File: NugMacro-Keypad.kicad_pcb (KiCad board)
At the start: 2 copper layers, 76.2 x 97.2 mm, 52 parts, among them J1 AVR-ISP-6, J2 Conn_01x04, J3 Conn_01x04_Female_For_LCD, SW1 SW_Push, SW2 RotaryEncoder_Switch, U1 ATmega32U4-A, Y1 16MHz

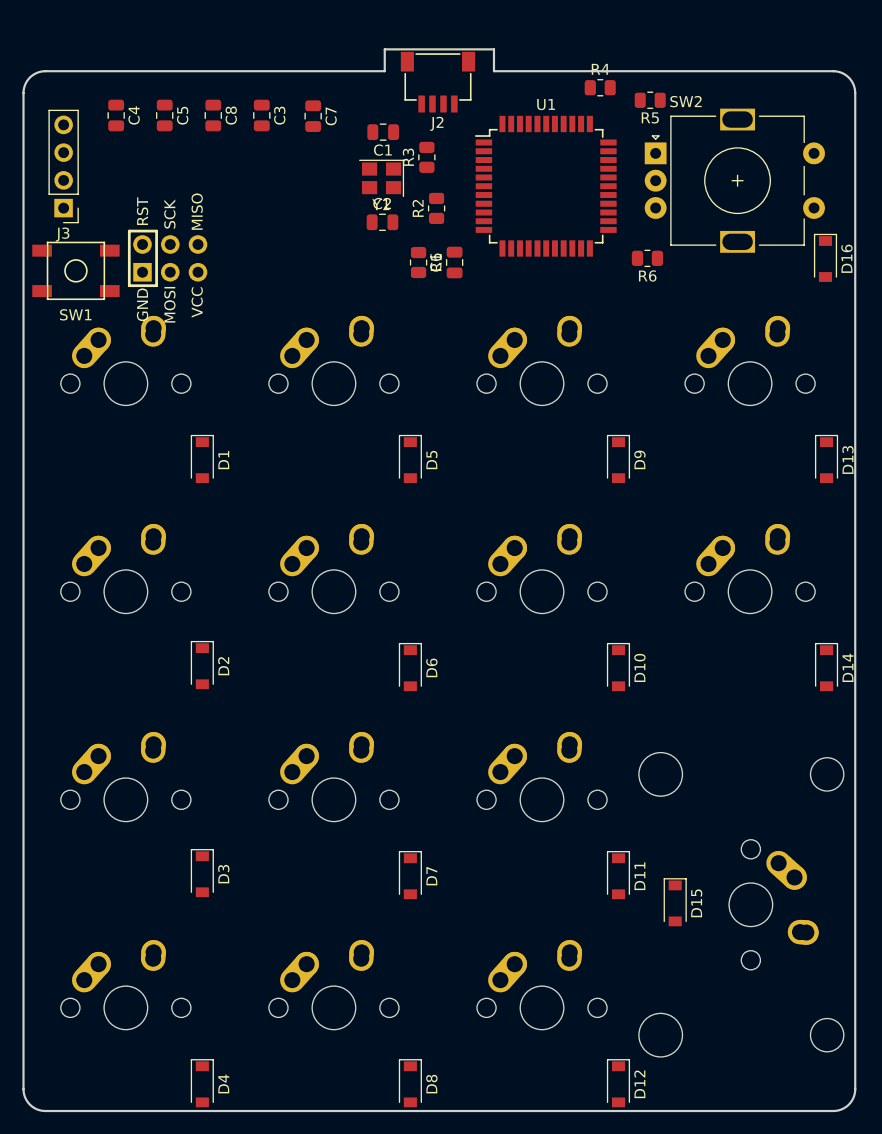
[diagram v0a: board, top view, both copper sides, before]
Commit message: lil schema and pcb changes
flipped/ changed around smd components so it may be easier to route, got rid of reset pins for simplicity sake with small board
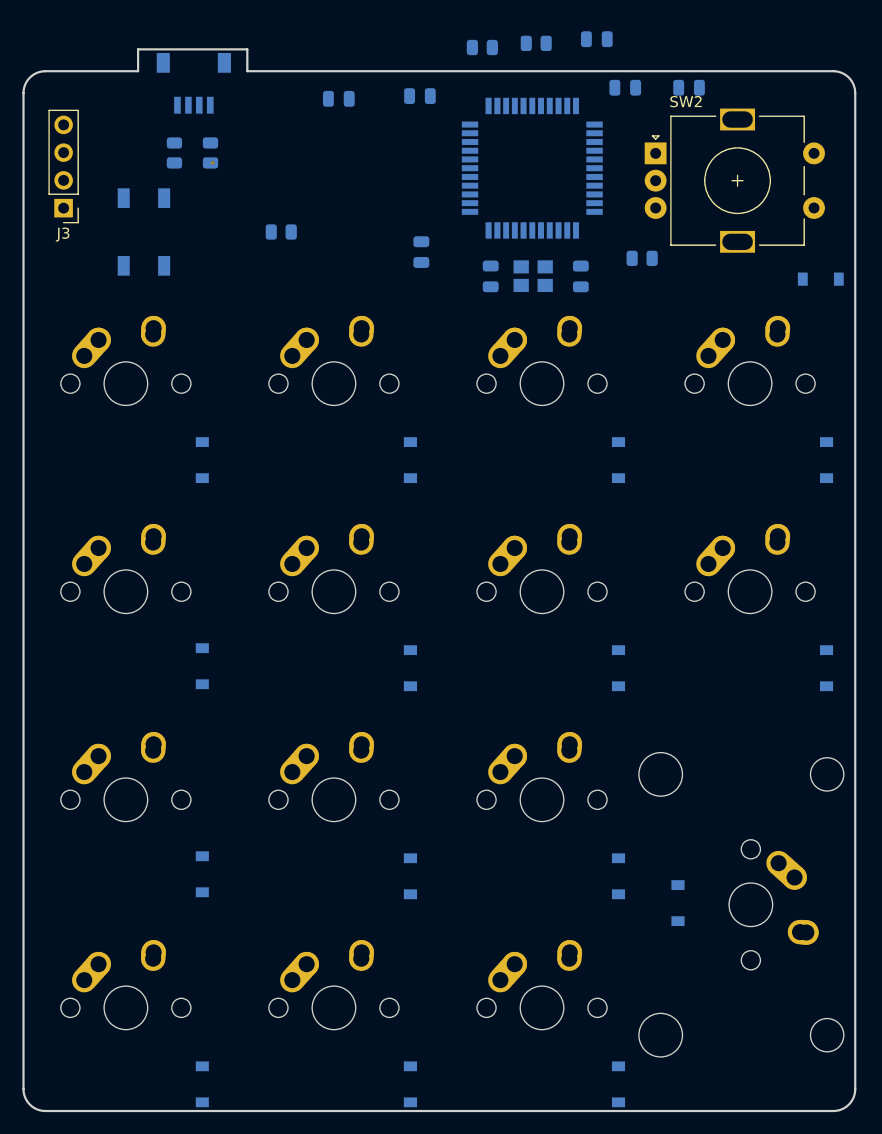
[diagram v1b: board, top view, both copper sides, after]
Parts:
- removed J1: AVR-ISP-6, random-keyboard-parts:Reset_Pretty-Mask
- C1, C2, C3, C4, C5, C6, C7, C8, D1, D10, D11, D12, D13, D14, D15, D16, D2, D3, D4, D5, D6, D7, D8, D9, J2, R1, R2, R3, R4, R5, R6, SW1, U1, Y1: moved to B.Cu
- moved C5 48.1 mm to (79.4, 57.3), turned to 180 degrees
- moved C3 31.5 mm to (70.9, 52.8), turned to 180 degrees
- moved C4 30.6 mm to (54.9, 72.3), turned to 90 degrees
- moved C7 28.7 mm to (73.5, 57.3), turned to 0 degrees
- moved R2 24.5 mm to (32.3, 63.2)
- moved J2 22.4 mm to (34.0, 54.1), turned to 0 degrees
- moved R3 19.8 mm to (35.6, 63.2)
- moved C2 18.8 mm to (69.5, 74.6), turned to 90 degrees
- moved Y1 16.5 mm to (65.1, 74.5)
- moved C1 16.5 mm to (61.2, 74.5), turned to -90 degrees
- moved R5 16.1 mm to (60.5, 53.6), turned to 0 degrees
- moved C6 15.6 mm to (54.7, 58.0), turned to 180 degrees
- moved R1 12.9 mm to (42.0, 70.5), turned to 180 degrees
- moved C8 11.6 mm to (47.3, 58.3), turned to 180 degrees
- moved SW1 7.17 mm to (29.5, 70.5), turned to 90 degrees
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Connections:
- net +5V renamed VCC
- U1 pad 10: MOSI -> unconnected-(U1-Pad10)
- U1 pad 11: MISO -> unconnected-(U1-Pad11)
- U1 pad 12: OLED2 -> unconnected-(U1-Pad12)
- U1 pad 22: unconnected-(U1-Pad22) -> COL0
- U1 pad 25: unconnected-(U1-Pad25) -> COL1
- U1 pad 26: unconnected-(U1-Pad26) -> COL2
- U1 pad 27: unconnected-(U1-Pad27) -> COL3
- U1 pad 28: DT -> unconnected-(U1-Pad28)
- U1 pad 30: OLED1 -> DT
- U1 pad 31: COL2 -> unconnected-(U1-Pad31)
- U1 pad 32: COL3 -> unconnected-(U1-Pad32)
- U1 pad 36: COL1 -> unconnected-(U1-Pad36)
- U1 pad 8: COL0 -> OLED1
- U1 pad 9: SCK -> OLED2
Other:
- outline, holes or cut-outs redrawn

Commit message: routing changes
routed keyswitch matrix. Have not done supporting components yet.
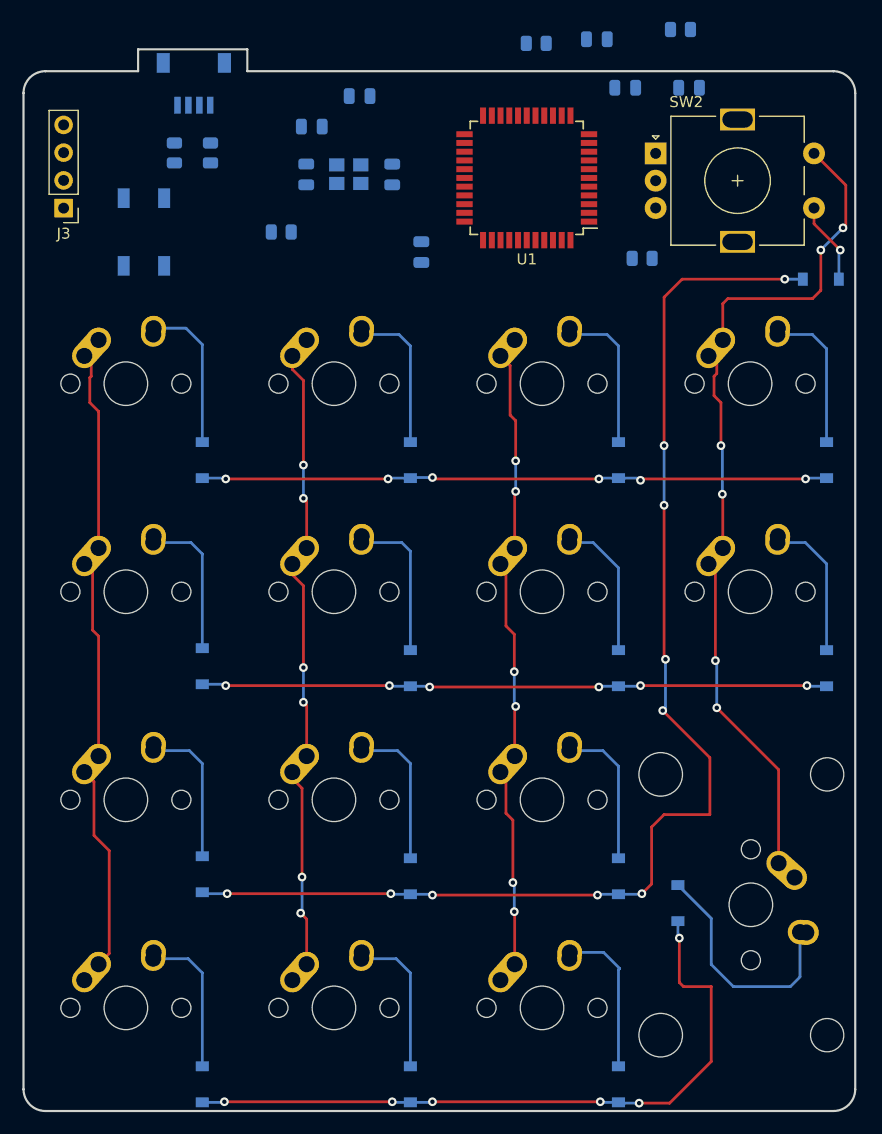
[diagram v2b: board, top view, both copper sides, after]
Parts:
- U1: moved to F.Cu
- moved C2 19.6 mm to (52.2, 65.2)
- moved Y1 19.3 mm to (48.2, 65.2)
- moved C1 19.3 mm to (44.3, 65.2)
- moved R5 18.2 mm to (78.6, 51.9), turned to 180 degrees
- moved C6 5.53 mm to (49.2, 58.0)
- moved C8 3.55 mm to (44.8, 60.8)
- moved U1 1.02 mm to (64.5, 65.5)
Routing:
- net ROW2: track 0.00 -> 115.4 mm, vias 0 -> 10
- net COL3: track 0.00 -> 75.9 mm, vias 0 -> 6
- net ROW3: track 0.00 -> 63.9 mm, vias 0 -> 6
- net ROW0: track 0.00 -> 57.5 mm, vias 0 -> 6
- net ROW1: track 0.00 -> 57.3 mm, vias 0 -> 6
- net COL0: track 0.00 -> 55.3 mm
- net COL2: track 0.00 -> 54.5 mm, vias 0 -> 6
- net COL1: track 0.00 -> 54.5 mm, vias 0 -> 6
- net Net-(D15-Pad2): track 0.00 -> 22.0 mm
- net Net-(D12-Pad2): track 0.00 -> 14.2 mm
- net Net-(D1-Pad2): track 0.00 -> 14.0 mm
- net Net-(D6-Pad2): track 0.00 -> 13.9 mm
- net Net-(D5-Pad2): track 0.00 -> 13.7 mm
- net Net-(D9-Pad2): track 0.00 -> 13.7 mm
- net Net-(D7-Pad2): track 0.00 -> 13.7 mm
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
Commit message: routing changes again
finished some routing going to change column/row flags hopefully works heres this if it dont.
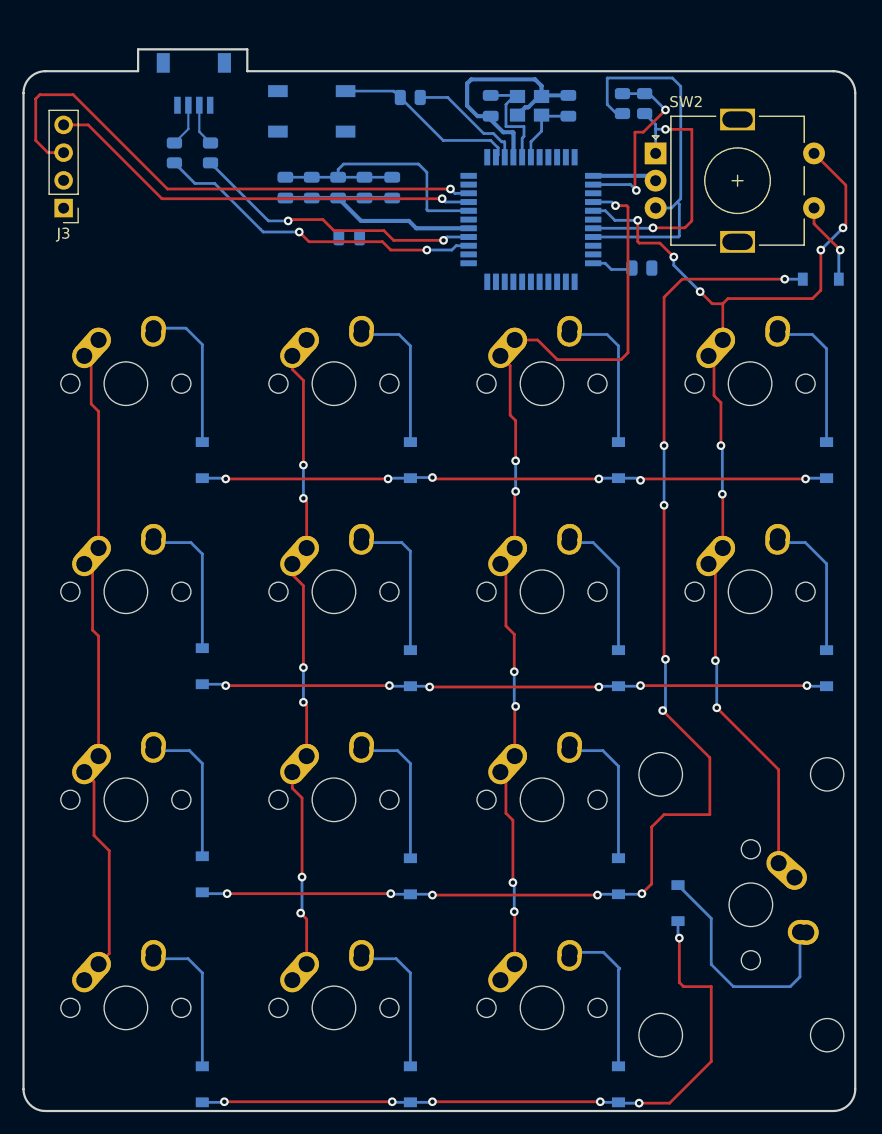
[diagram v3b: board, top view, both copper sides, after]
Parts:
- U1: moved to B.Cu
- moved C3 31.6 mm to (42.4, 66.4), turned to -90 degrees
- moved C5 31.1 mm to (49.7, 66.4), turned to -90 degrees
- moved C1 24.8 mm to (68.3, 58.9), turned to 90 degrees
- moved C7 23.2 mm to (52.2, 66.4), turned to -90 degrees
- moved R4 22.7 mm to (75.1, 73.8)
- moved SW1 18.9 mm to (44.8, 59.4), turned to 180 degrees
- moved Y1 17.7 mm to (64.8, 58.9)
- moved R1 17.1 mm to (53.8, 58.2)
- moved R6 14.3 mm to (73.3, 58.7), turned to 90 degrees
- moved C6 13.0 mm to (48.3, 71.0)
- moved C4 11.6 mm to (44.8, 66.4), turned to -90 degrees
- moved C2 11.0 mm to (61.2, 58.9), turned to -90 degrees
- moved R5 7.54 mm to (75.3, 58.7), turned to 90 degrees
- moved C8 6.09 mm to (47.2, 66.4), turned to -90 degrees
- moved U1 3.83 mm to (64.9, 69.3), turned to 0 degrees
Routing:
- net VCC: track 0.00 -> 55.0 mm, vias 0 -> 2
- net GND: track 0.00 -> 52.1 mm
- net OLED2: track 0.00 -> 50.4 mm, vias 0 -> 1
- net OLED1: track 0.00 -> 40.0 mm, vias 0 -> 1
- net DT: track 0.00 -> 35.3 mm
- net Net-(R2-Pad1): track 0.00 -> 30.4 mm, vias 0 -> 2
- net COL2: track 54.5 -> 82.6 mm, vias 6 -> 7
- net Net-(R3-Pad1): track 0.00 -> 26.8 mm, vias 0 -> 2
- net CLK: track 0.00 -> 25.1 mm, vias 0 -> 2
- net RESET: track 0.00 -> 17.1 mm
- net COL3: track 75.9 -> 92.7 mm, vias 6 -> 9
- net XTAL2: track 0.45 -> 10.9 mm
- net XTAL1: track 0.00 -> 6.76 mm
- net D-: track 0.00 -> 3.99 mm
- net D+: track 0.00 -> 3.88 mm
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
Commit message: First prototype pcb done
finally
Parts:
- moved C6 5.89 mm to (53.9, 69.3)
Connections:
- net VCC renamed +5V
- U1 pad 18: ROW0 -> unconnected-(U1-Pad18)
- U1 pad 19: ROW1 -> unconnected-(U1-Pad19)
- U1 pad 20: ROW2 -> unconnected-(U1-Pad20)
- U1 pad 21: ROW3 -> unconnected-(U1-Pad21)
- U1 pad 22: COL0 -> unconnected-(U1-Pad22)
- U1 pad 25: COL1 -> unconnected-(U1-Pad25)
- U1 pad 36: unconnected-(U1-Pad36) -> COL1
- U1 pad 37: unconnected-(U1-Pad37) -> COL0
- U1 pad 38: unconnected-(U1-Pad38) -> ROW0
- U1 pad 39: unconnected-(U1-Pad39) -> ROW1
- U1 pad 40: unconnected-(U1-Pad40) -> ROW2
- U1 pad 41: unconnected-(U1-Pad41) -> ROW3
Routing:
- net +5V: track 55.0 -> 186.7 mm, vias 2 -> 7
- net ROW3: track 63.9 -> 194.9 mm
- net ROW2: track 115.4 -> 227.8 mm
- net ROW1: track 57.3 -> 151.5 mm
- net GND: track 52.1 -> 138.6 mm, vias 0 -> 3
- net ROW0: track 57.5 -> 136.7 mm
- net COL0: track 55.2 -> 102.1 mm
- net COL1: track 54.5 -> 82.6 mm, vias 6 -> 7
- net Net-(C6-Pad1): track 0.00 -> 4.34 mm

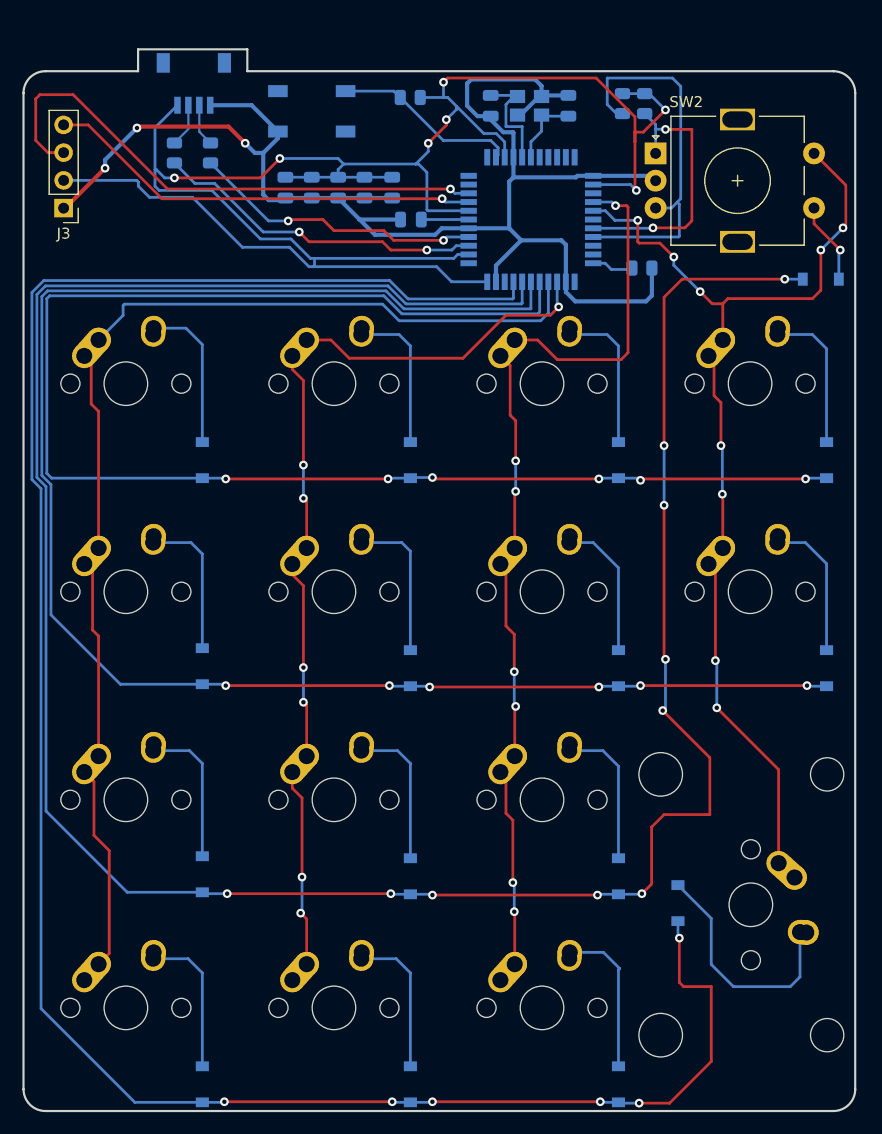
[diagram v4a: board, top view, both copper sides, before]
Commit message: finished pcb aside from silkscreen
next update will be of silkscreen design but as of now pcb is ready for plotting.
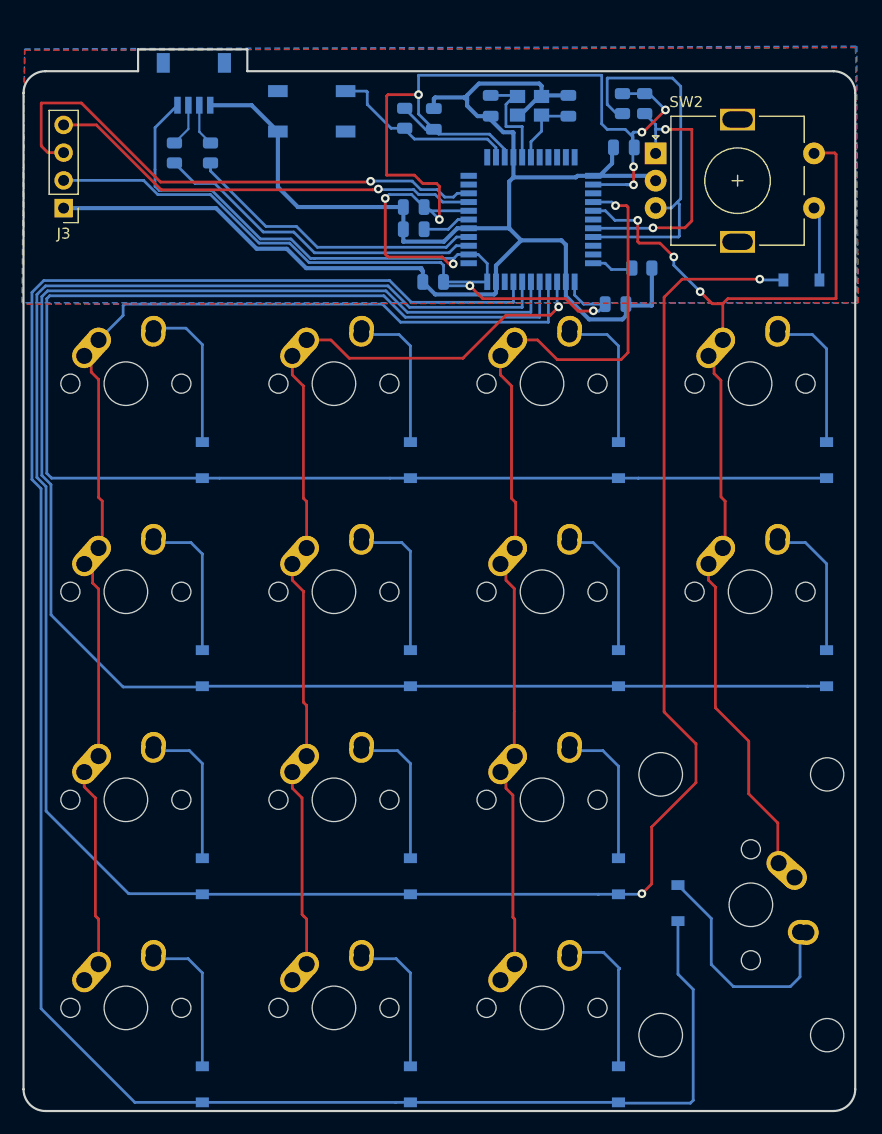
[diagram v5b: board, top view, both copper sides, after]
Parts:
- moved C8 27.5 mm to (72.6, 77.1), turned to 0 degrees
- moved C5 24.0 mm to (73.4, 62.7), turned to 180 degrees
- moved C4 12.8 mm to (56.0, 60.1), turned to 90 degrees
- moved C3 11.9 mm to (54.2, 68.2), turned to 180 degrees
- moved C7 9.41 mm to (55.9, 75.1), turned to 180 degrees
- moved R1 1.97 mm to (53.3, 60.1), turned to -90 degrees
- moved D16 1.78 mm to (89.7, 74.9)
- moved C6 0.93 mm to (54.2, 70.2)
- moved D3 0.18 mm to (34.8, 129.5)
- moved D2 0.18 mm to (34.8, 110.4)
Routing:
- net GND: track 138.6 -> 161.2 mm, vias 3 -> 0
- net +5V: track 186.7 -> 208.5 mm, vias 7 -> 10
- net ROW2: track 227.8 -> 222.9 mm, vias 10 -> 2
- net COL3: track 92.7 -> 94.5 mm, vias 9 -> 3
- net ROW3: track 194.9 -> 193.5 mm, vias 6 -> 0
- net OLED2: track 50.4 -> 49.2 mm
- net Net-(R3-Pad1): track 26.8 -> 27.7 mm, vias 2 -> 0
- net Net-(D16-Pad2): track 7.56 -> 6.80 mm, vias 1 -> 0
- net ROW1: track 151.5 -> 151.9 mm, vias 6 -> 0
- net Net-(R2-Pad1): track 30.4 -> 30.6 mm, vias 2 -> 0
- net ROW0: track 136.7 -> 136.9 mm, vias 6 -> 0
- net COL2: track 82.6 -> 82.5 mm, vias 7 -> 1
- net COL1: track 82.6 -> 82.5 mm, vias 7 -> 1
- added copper zone on B.Cu, net GND
- added copper zone on F.Cu, net GND
